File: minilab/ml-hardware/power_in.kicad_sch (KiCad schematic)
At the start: 1 part, among them J7 Molex lite-trap

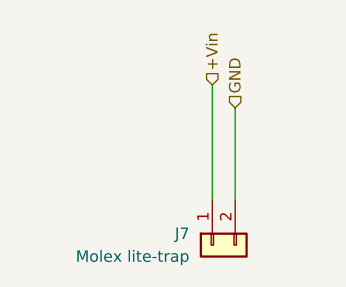
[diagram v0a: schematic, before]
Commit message: minilab: Agrega 2da opc conectores y modelos 3d
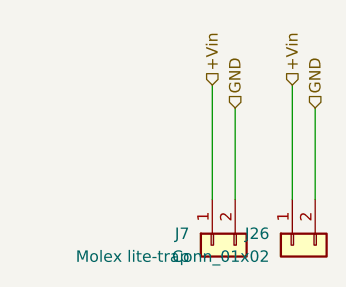
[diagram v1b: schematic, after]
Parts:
- added J26: Conn_01x02, Connector_PinSocket_2.54mm:PinSocket_1x02_P2.54mm_Horizontal, symbol Connector_Generic:Conn_01x02
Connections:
- net +Vin: now also J26.1 (Pin_1)
- net GND: now also J26.2 (Pin_2)
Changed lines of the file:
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@@
+	(wire
+		(pts
+			(xy 151.13 90.17) (xy 151.13 100.33)
+		)
+		(stroke
+			(width 0)
+			(type default)
+		)
+	)
 	(wire
 		(pts
@@
 			(width 0)
 			(type default)
+		)
+	)
+	(wire
+		(pts
+			(xy 148.59 87.63) (xy 148.59 100.33)
+		)
+		(stroke
+			(width 0)
+			(type default)
+		)
+	)
+	(hierarchical_label "GND"
+		(shape input)
+		(at 151.13 90.17 90)
+		(effects
+			(font
+				(size 1.27 1.27)
+			)
+			(justify left)
 		)
 	)
@@
 		)
 	)
+	(hierarchical_label "+Vin"
+		(shape input)
+		(at 148.59 87.63 90)
+		(effects
+			(font
+				(size 1.27 1.27)
+			)
+			(justify left)
+		)
+	)
+	(symbol
+		(lib_id "Connector_Generic:Conn_01x02")
+		(at 148.59 105.41 90)
+		(mirror x)
+		(unit 1)
+		(exclude_from_sim no)
+		(in_bom yes)
+		(on_board yes)
+		(dnp no)
+		(property "Reference" "J26"
+			(at 146.05 104.1399 90)
+			(effects
+				(font
+					(size 1.27 1.27)
+				)
+				(justify left)
+			)
+		)
+		(property "Value" "Conn_01x02"
+			(at 146.05 106.6799 90)
+			(effects
+				(font
+					(size 1.27 1.27)
+				)
+				(justify left)
+			)
+		)
+		(property "Footprint" "Connector_PinSocket_2.54mm:PinSocket_1x02_P2.54mm_Horizontal"
+			(at 148.59 105.41 0)
+			(effects
+				(font
+					(size 1.27 1.27)
+				)
+				(hide yes)
+			)
+		)
+		(property "Datasheet" "~"
+			(at 148.59 105.41 0)
+			(effects
+				(font
+					(size 1.27 1.27)
+				)
+				(hide yes)
+			)
+		)
+		(property "Description" "Generic connector, single row, 01x02, script generated (kicad-library-utils/schlib/autogen/connector/)"
+			(at 148.59 105.41 0)
+			(effects
+				(font
+					(size 1.27 1.27)
+				)
+				(hide yes)
+			)
+		)
+		(pin "2"
+		)
+		(pin "1"
+		)
+		(instances
+			(project ""
+				(path "/edb8a0df-1def-48df-b494-4a6b89ce8f9c/50d494f2-d484-43a0-8d2a-b6d7f45e4af0"
+					(reference "J26")
+					(unit 1)
+				)
+			)
+		)
+	)

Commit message: minilab: Corrige huella molex microfit y edge-*-02
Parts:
- J7: footprint Extras:104238-0210 -> Extras:Molex-Lite_trap
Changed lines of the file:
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@@
 			)
 		)
-		(property "Footprint" "Extras:104238-0210"
+		(property "Footprint" "Extras:Molex-Lite_trap"
 			(at 139.7 105.41 0)
 			(effects
